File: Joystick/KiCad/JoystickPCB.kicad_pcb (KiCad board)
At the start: 2 copper layers, 62 x 28 mm, 22 parts, among them J1 B4B-PH-SM4-TBT, J2 B4B-PH-SM4-TBT, U2 ADS1115IDGSR, U3 ICM-20948, U4 MIC5225-1.8YM5-TR

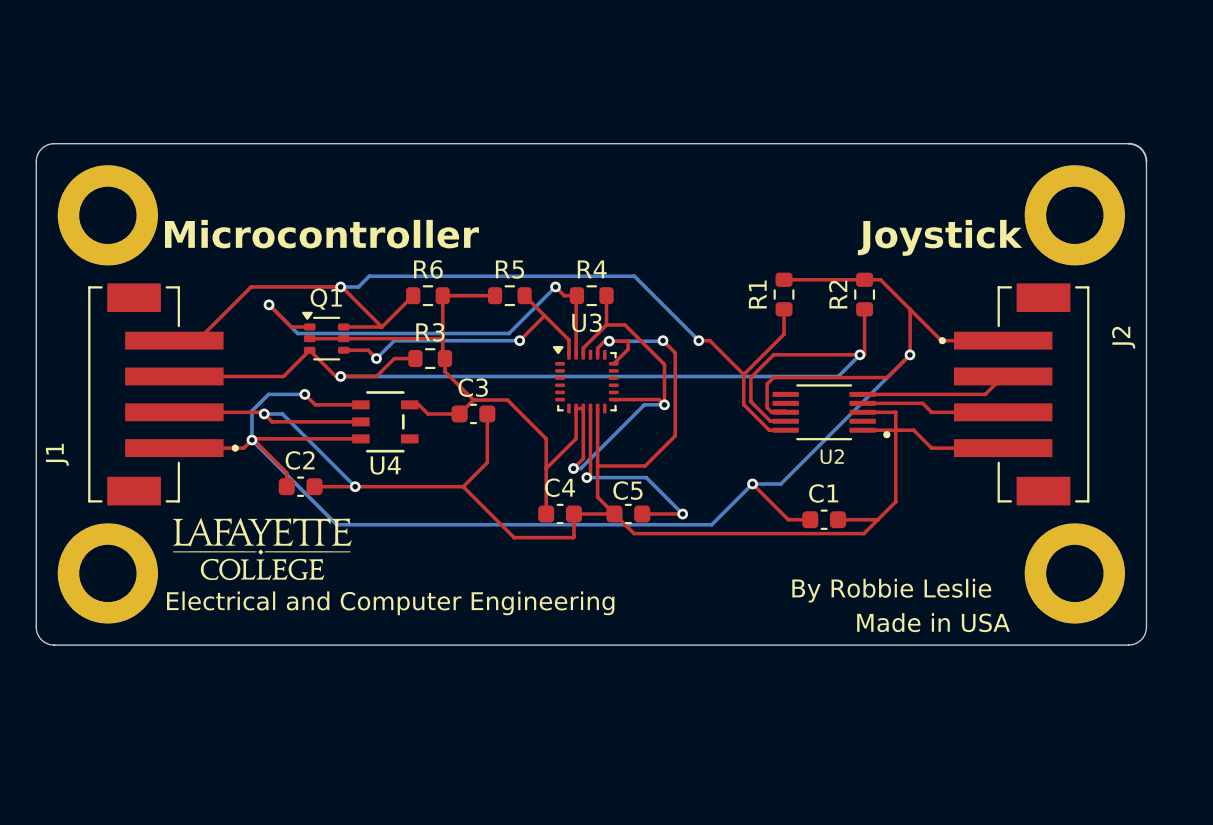
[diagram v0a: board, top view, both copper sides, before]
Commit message: Redesigned PCB with new connectors
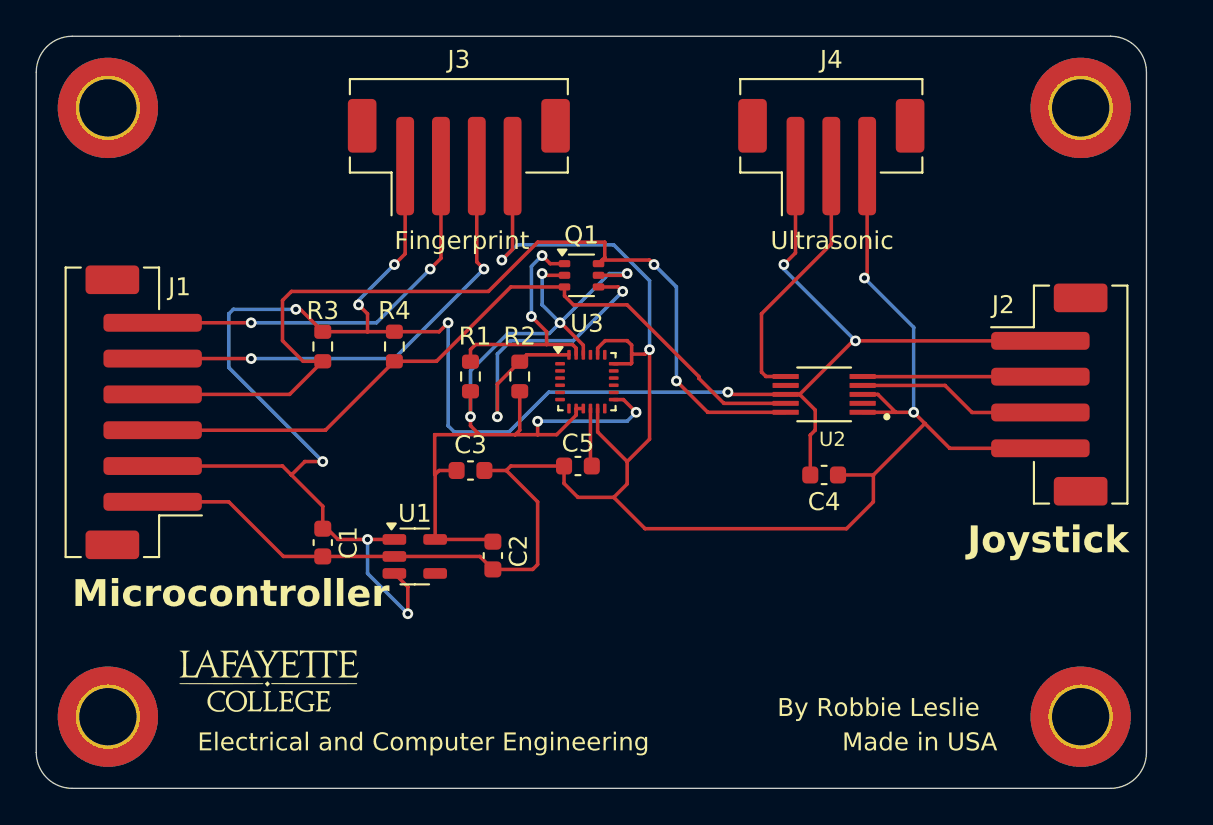
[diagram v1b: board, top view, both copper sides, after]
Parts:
- removed R5, R6: 10k, Resistor_SMD:R_0603_1608Metric
- removed REF** (x4): MountingHole_3.2mm_M3_DIN965_Pad, MountingHole:MountingHole_3.2mm_M3_DIN965_Pad
- removed U4: MIC5225-1.8YM5-TR, Library:SOT-23-5_M5_MCH
- added H1: MountingHole, MountingHole:MountingHole_3.2mm_M3_DIN965_Pad_TopBottom, F.Cu at (130.0, 51.0)
- added H2: MountingHole, MountingHole:MountingHole_3.2mm_M3_DIN965_Pad_TopBottom, F.Cu at (184.3, 51.0)
- added H3: MountingHole, MountingHole:MountingHole_3.2mm_M3_DIN965_Pad_TopBottom, F.Cu at (130.0, 85.0)
- added H4: MountingHole, MountingHole:MountingHole_3.2mm_M3_DIN965_Pad_TopBottom, F.Cu at (184.3, 85.0)
- added J3: JST B4B-PH-SM4-TB, Connector_JST:JST_PH_B4B-PH-SM4-TB_1x04-1MP_P2.00mm_Vertical, F.Cu at (149.6, 53.8)
- added J4: JST B3B-PH-SM4-TB, Connector_JST:JST_PH_B3B-PH-SM4-TB_1x03-1MP_P2.00mm_Vertical, F.Cu at (170.4, 53.8)
- added U1: MIC5225-1.8YM5-TR, Package_TO_SOT_SMD:SOT-23-5, F.Cu at (147.1, 76.0)
- C3: value 10uF -> 0.1uF
- C4: value 0.1uF -> 10uF
- J1: value B4B-PH-SM4-TBT -> JST B6B-PH-SM4-TB; footprint Library:JST_B4B-PH-SM4-TBT -> Connector_JST:JST_PH_B6B-PH-SM4-TB_1x06-1MP_P2.00mm_Vertical
- J2: value B4B-PH-SM4-TBT -> JST B4B-PH-SM4-TB; footprint Library:JST_B4B-PH-SM4-TBT -> Connector_JST:JST_PH_B4B-PH-SM4-TB_1x04-1MP_P2.00mm_Vertical
- R1, R2, R3, R4: value 10k -> 4.7k
- moved C1 28.0 mm to (142.0, 75.3), turned to -90 degrees
- moved R2 19.8 mm to (153.0, 66.0)
- moved R1 18.1 mm to (150.2, 66.0)
- moved C4 14.9 mm to (170.0, 71.5)
- moved Q1 14.7 mm to (156.4, 60.4)
- moved C2 11.4 mm to (151.5, 76.0), turned to -90 degrees
- moved R4 11.4 mm to (146.0, 64.3), turned to 90 degrees
- moved G*** 7.37 mm to (139.0, 83.0)
- moved R3 6.04 mm to (142.0, 64.3), turned to 90 degrees
- moved C5 3.89 mm to (156.2, 71.0)
- moved C3 3.16 mm to (150.2, 71.2)
- moved J1 1.14 mm to (132.0, 68.0)
- moved U2 1.00 mm to (170.0, 67.0)
- moved J2 0.33 mm to (182.6, 67.0)
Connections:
- C2 pad 1: /3.3V -> /1.8V
- C4 pad 1: /1.8V -> /3.3V
- J1 pad 1: /3.3V -> /GND
- J1 pad 2: /GND -> /3.3V
- R1 pad 1: /SCL -> /1.8V
- R1 pad 2: /3.3V -> /SCL_1.8V
- R2 pad 1: /SDA -> /1.8V
- R2 pad 2: /3.3V -> /SDA_1.8V
- R3 pad 1: /SDA -> /SCL
- R3 pad 2: /1.8V -> /3.3V
- R4 pad 1: /1.8V -> /SDA
- R4 pad 2: /SCL_1.8V -> /3.3V
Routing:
- net /GND: track 99.2 -> 126.3 mm
- net /RX: track 0.00 -> 26.5 mm, vias 0 -> 2
- net /TX: track 0.00 -> 22.7 mm, vias 0 -> 2
- net /3.3V: track 97.1 -> 117.7 mm, vias 4 -> 10
- net /SDA: track 57.7 -> 41.7 mm, vias 2 -> 0
- net /A2: track 0.00 -> 14.6 mm
- net /SCL_1.8V: track 25.2 -> 14.2 mm
- net Net-(U3-REGOUT): track 12.4 -> 3.24 mm, vias 2 -> 0
- net /1.8V: track 58.0 -> 54.7 mm, vias 2 -> 6
- net /SDA_1.8V: track 16.7 -> 19.9 mm
- net /A0: track 8.06 -> 10.6 mm
- net /A1: track 8.26 -> 9.93 mm
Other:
- board size 62 x 28 mm -> 62 x 42 mm
- board text added: "Fingerprint"
- board text added: "Ultrasonic"

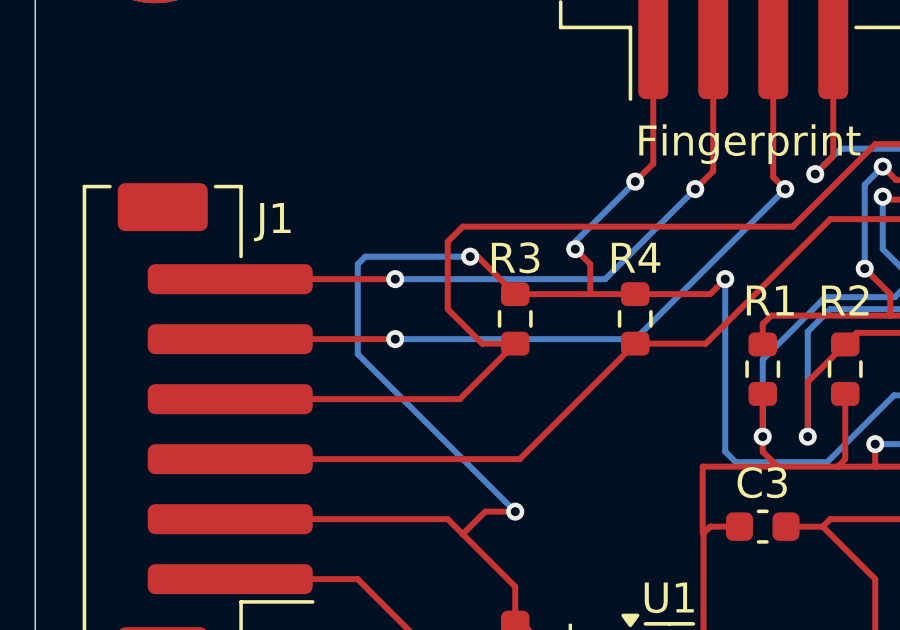
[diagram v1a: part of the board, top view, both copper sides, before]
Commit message: Removed I2C pullups since they will go on the main board
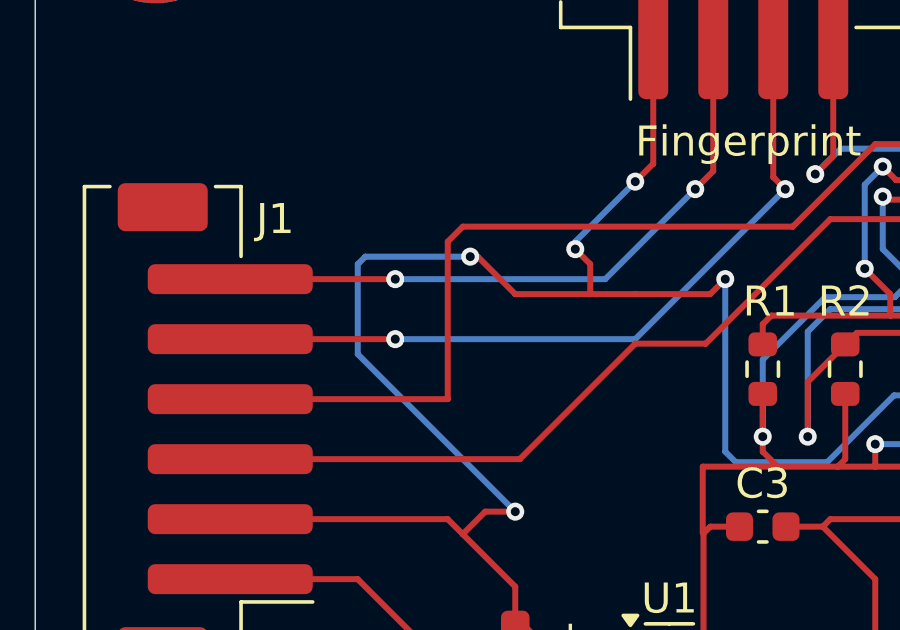
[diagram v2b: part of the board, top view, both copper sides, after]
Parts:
- removed R3, R4: 4.7k, Resistor_SMD:R_0603_1608Metric
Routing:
- net /SCL: track 53.1 -> 50.3 mm
